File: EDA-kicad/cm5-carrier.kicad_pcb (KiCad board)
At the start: 6 copper layers, 82 x 155 mm, 122 parts, among them J1 USBC-4-0-CX90MW9-24P1, J2 SIM-G85D1160022HHR, J3 FINGER, J4 SJ2-35894B-SMT-TR, SW1 EG25-switch-CSS-1210MC, SW2 MIC-switch-CSS-1210MC, SW3 CAM-switch-CSS-1210MC, SW4 PROG, SW5 VOL-, SW6 VOL+, SW7 POW, U10 Flash-LED-Lumiled, U2 EG25GGC-128-SGNS, U3 CODEC-TLV320AIC3204IRHBR, U4 BQ25792RQMR, U5 TPS650250RHBR, U6 BAT-CONNECTOR-FLTS22WR00, U7 22V-boost-AP3032KTR-G1, U8 MP3429GL-Z, U9 FPC15pin-1mm-pitch-F52Q-1A7H1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

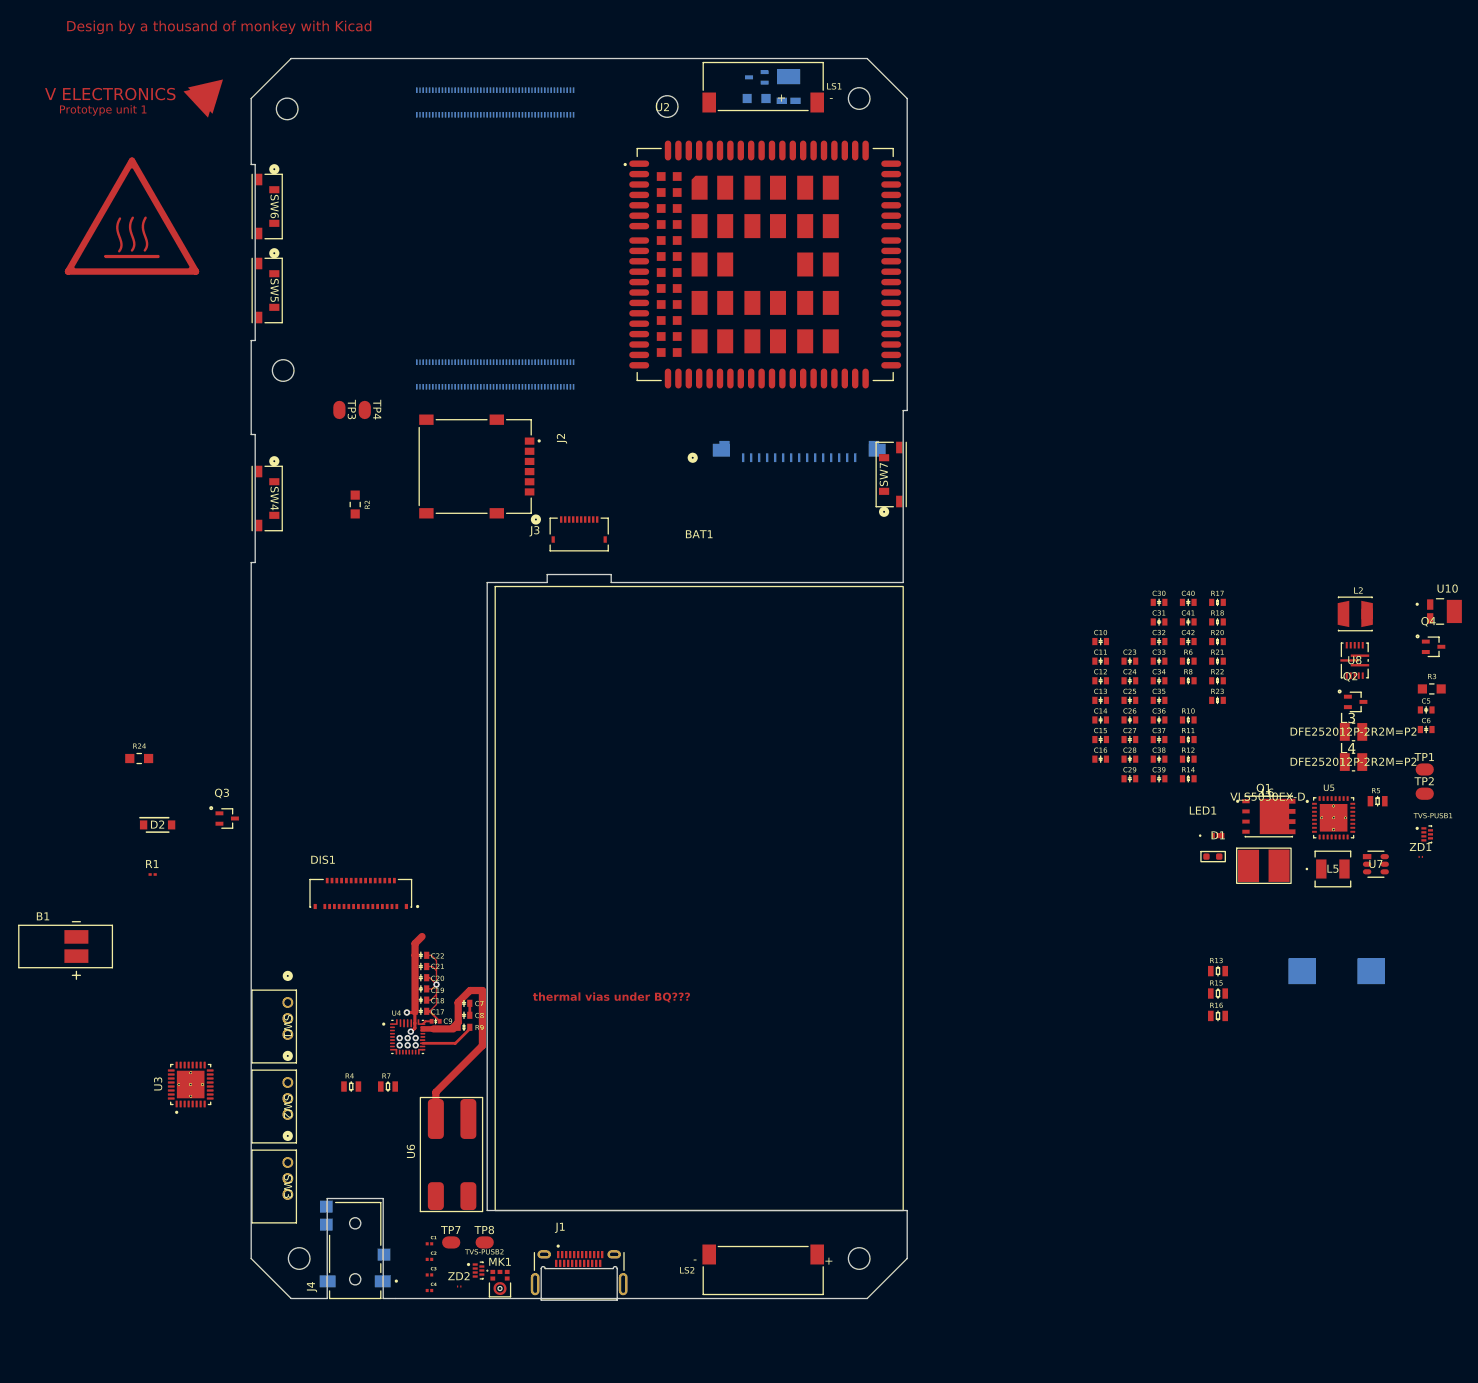
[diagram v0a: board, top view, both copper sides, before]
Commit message: charger 50% routed
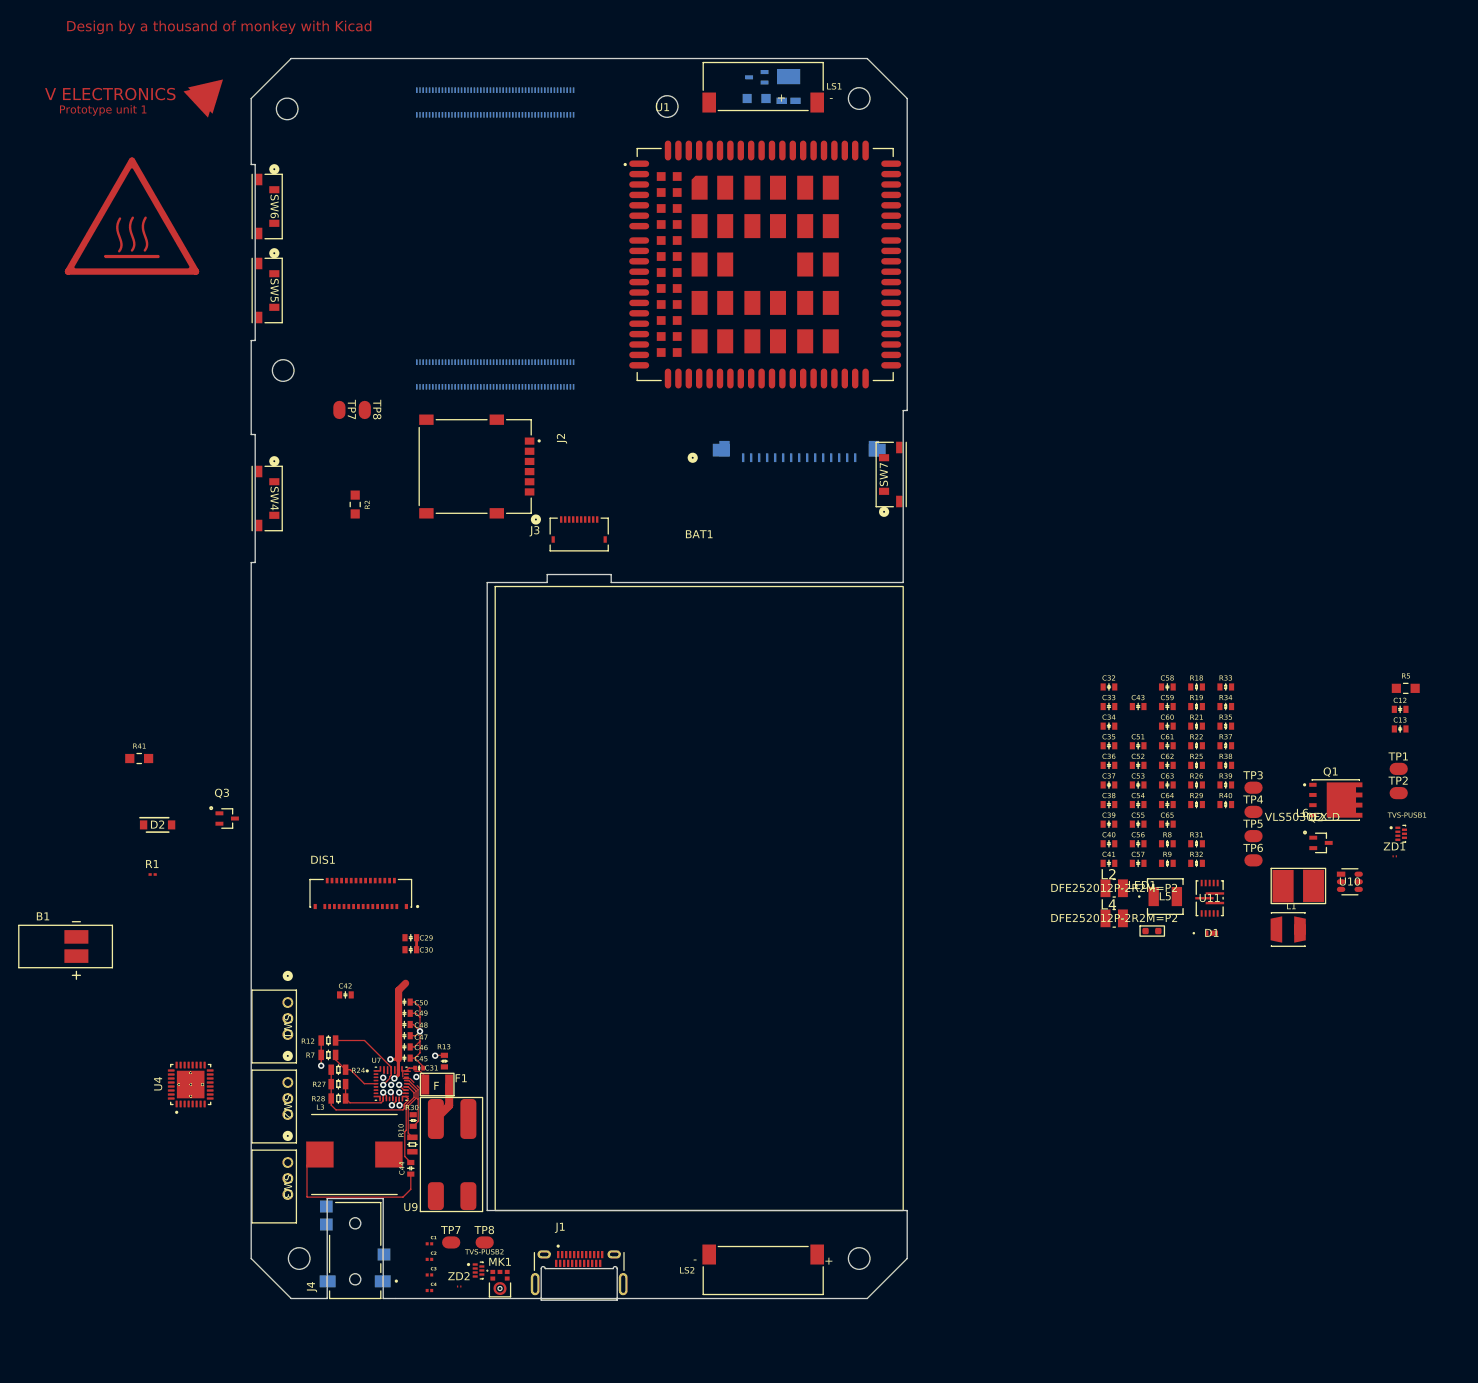
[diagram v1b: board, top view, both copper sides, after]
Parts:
- removed C10: 4.7μF, SPIRIT-footprints:0603-capacitor
- removed C11: 0.1μF, SPIRIT-footprints:0603-capacitor
- removed C14, C24, C25, C26, C27, C28: 10μF, SPIRIT-footprints:0603-capacitor
- removed C15, C16: 47nF, SPIRIT-footprints:0603-capacitor
- removed C23: 1μF, SPIRIT-footprints:0603-capacitor
- removed the C29 at (163.8, 121.0)
- removed the C30 at (167.5, 99.0)
- removed the C31 at (167.5, 101.4)
- removed C5: 200-pf-CC0603KRX7R7BB104, SPIRIT-footprints:0603-capacitor
- removed C6: 01-uf-CC0603KRX7R7BB104, SPIRIT-footprints:0603-capacitor
- removed the Q4 at (201.8, 104.5)
- removed R11: 1M, SPIRIT-footprints:0603-resistor
- removed the R12 at (171.1, 118.6)
- removed the R13 at (174.8, 145.1)
- removed R14: 10k, SPIRIT-footprints:0603-resistor
- removed R15: 10k, SPIRIT-footprints:0805-resistor
- removed R16: 30k, SPIRIT-footprints:0805-resistor
- removed R17: 680, SPIRIT-footprints:0603-resistor
- removed R20: 5, SPIRIT-footprints:0603-resistor
- removed R23: 6.8k, SPIRIT-footprints:0603-resistor
- removed R3: 100K-0805-resistor-ERA6AEB104V, SPIRIT-footprints:100K-0805-resistor-RES_ERA6AEB104V
- removed R6: 820k, SPIRIT-footprints:0603-resistor
- removed U5: TPS650250RHBR, SPIRIT-footprints:TPS650250-IC_ADS125H01IRHBT
- removed the U7 at (194.6, 131.7)
- removed U8: MP3429GL-Z, SPIRIT-footprints:QFN-3x4_MP3429_MNP
- added C43: 22uF, SPIRIT-footprints:0603-capacitor, F.Cu at (164.9, 112.0)
- added C44: 47nF, SPIRIT-footprints:0603-capacitor, F.Cu at (74.0, 169.7)
- added C51: 22uF, SPIRIT-footprints:0603-capacitor, F.Cu at (164.9, 116.9)
- added C52: 4.7uF, SPIRIT-footprints:0603-capacitor, F.Cu at (164.9, 119.4)
- added C53: 1uF, SPIRIT-footprints:0603-capacitor, F.Cu at (164.9, 121.8)
- added C54: 1uF, SPIRIT-footprints:0603-capacitor, F.Cu at (164.9, 124.3)
- added C55: 0.1uF, SPIRIT-footprints:0603-capacitor, F.Cu at (164.9, 126.7)
- added C56: 22uF, SPIRIT-footprints:0603-capacitor, F.Cu at (164.9, 129.2)
- added C57: 22uF, SPIRIT-footprints:0603-capacitor, F.Cu at (164.9, 131.6)
- added C58: 22uF, SPIRIT-footprints:0603-capacitor, F.Cu at (168.5, 109.6)
- added C59: 0.1uF, SPIRIT-footprints:0603-capacitor, F.Cu at (168.5, 112.0)
- added C60: 22uF, SPIRIT-footprints:0603-capacitor, F.Cu at (168.5, 114.5)
- added C61: 22uF, SPIRIT-footprints:0603-capacitor, F.Cu at (168.5, 116.9)
- added C62: 22uF, SPIRIT-footprints:0603-capacitor, F.Cu at (168.5, 119.4)
- added C63: 6.8nF, SPIRIT-footprints:0603-capacitor, F.Cu at (168.5, 121.8)
- added C64: 4.7uF, SPIRIT-footprints:0603-capacitor, F.Cu at (168.5, 124.3)
- added C65: 22uF, SPIRIT-footprints:0603-capacitor, F.Cu at (168.5, 126.7)
- added F1: 9A 6V, SPIRIT-footprints:PTC RESET FUSE 9.0A 6V 1210 1210L900SLPR, F.Cu at (77.2, 161.1)
- added R19: 680kΩ 1%, SPIRIT-footprints:0603-resistor, F.Cu at (172.2, 112.0)
- added R24: 5.23kΩ, SPIRIT-footprints:0805-resistor, F.Cu at (64.9, 157.4)
- added R25: 10kΩ, SPIRIT-footprints:0603-resistor, F.Cu at (172.2, 119.4)
- added R26: 470kΩ 1%, SPIRIT-footprints:0603-resistor, F.Cu at (172.2, 121.8)
- added R27: 10kΩ, SPIRIT-footprints:0805-resistor, F.Cu at (64.9, 159.2)
- added R28: 30kΩ, SPIRIT-footprints:0805-resistor, F.Cu at (64.9, 161.0)
- added R29: 680Ω, SPIRIT-footprints:0603-resistor, F.Cu at (172.2, 124.3)
- added R30: 10kΩ, SPIRIT-footprints:0603-resistor, F.Cu at (74.2, 163.8)
- added R31: 100kΩ, SPIRIT-footprints:0603-resistor, F.Cu at (172.2, 129.2)
- added R32: 100kΩ, SPIRIT-footprints:0603-resistor, F.Cu at (172.2, 131.6)
- added R33: 100kΩ, SPIRIT-footprints:0603-resistor, F.Cu at (175.8, 109.6)
- added R34: 820kΩ, SPIRIT-footprints:0603-resistor, F.Cu at (175.8, 112.0)
- added R35: 182KΩ, SPIRIT-footprints:0603-resistor, F.Cu at (175.8, 114.5)
- added R37: 5Ω, SPIRIT-footprints:0603-resistor, F.Cu at (175.8, 116.9)
- added R38: 750kΩ, SPIRIT-footprints:0603-resistor, F.Cu at (175.8, 119.4)
- added R39: 200kΩ, SPIRIT-footprints:0603-resistor, F.Cu at (175.8, 121.8)
- added R40: 6.8kΩ, SPIRIT-footprints:0603-resistor, F.Cu at (175.8, 124.3)
- added R9: 10k, SPIRIT-footprints:0603-resistor, F.Cu at (168.5, 131.6)
- added TP3: test-pad-1, SPIRIT-footprints:test-pad-1, F.Cu at (179.3, 121.1)
- added TP4: test-pad-1, SPIRIT-footprints:test-pad-1, F.Cu at (179.3, 124.2)
- added TP5: test-pad-1, SPIRIT-footprints:test-pad-1, F.Cu at (179.3, 127.2)
- added TP6: test-pad-1, SPIRIT-footprints:test-pad-1, F.Cu at (179.3, 130.2)
- added U11: MP3429GL-Z, SPIRIT-footprints:QFN-3x4_MP3429_MNP, F.Cu at (173.8, 136.0)
- C12: value 10μF -> 200pF
- C13: value 10μF -> 0.1uF
- C29: renamed from C7; value 10μF -> 10uF
- C30: renamed from C8; value 10μF -> 10uF
- C32: value 0.1μF -> 1uF
- C33, C34, C35, C39: value 22μF -> 10uF
- C36: value 0.1μF -> 22uF
- C37: value 22μF -> 4.7uF
- C38: value 22μF -> 0.1uF
- C40: value 6.8nF -> 10uF
- C41: value 4.7μF -> 10uF
- C42: value 22μF -> 47nF
- C45: renamed from C17; value 0.1μF -> 0.1uF
- C46: renamed from C18; value 10μF -> 10uF
- C47: renamed from C19; value 10μF -> 10uF
- C48: renamed from C20; value 10μF -> 10uF
- C49: renamed from C21; value 10μF -> 10uF
- C50: renamed from C22; value 10μF -> 10uF
- L1: value 2.2uH -> 3.3uH; footprint SPIRIT-footprints:2-2uh-inductorIND_ETQP4M2R2KVC -> SPIRIT-footprints:3-3uH-MURATA_LQH44PN3R3MPRL; moved to F.Cu
- L2: value 3.3uH -> 2.2uH; footprint SPIRIT-footprints:3-3uH-MURATA_LQH44PN3R3MPRL -> SPIRIT-footprints:2-2uH-inductor-INDC2520X120N
- L3: footprint SPIRIT-footprints:2-2uH-inductor-INDC2520X120N -> SPIRIT-footprints:2-2uh-inductorIND_ETQP4M2R2KVC
- R10: value 182K -> 4.7KΩ; footprint SPIRIT-footprints:0603-resistor -> SPIRIT-footprints:0805-resistor
- R12: renamed from R7; value 100k -> 100kΩ
- R13: renamed from R9; value 100 -> 100Ω
- R18: value 10k -> 100kΩ
- R2: value 270K-05W-0805-RES_ERJP06J102V -> 270KΩ 0.5W
- R21: value 750k -> 470kΩ 1%
- R22: value 200k -> 1MΩ 1%
- R41: renamed from R24; value 1K-05W-0805-RES_ERJP06J102V -> 1KΩ 0.5W
- R42: renamed from R25; value 1K -> 1KΩ 0.5W
- R5: value 4.7K -> 100KΩ; footprint SPIRIT-footprints:0805-resistor -> SPIRIT-footprints:100K-0805-resistor-RES_ERA6AEB104V
- R7: renamed from R4; value 127k -> 127kΩ
- R8: value 47k -> 10k
- U10: value Flash-LED-Lumiled -> 22V-boost-AP3032KTR-G1; footprint SPIRIT-footprints:LUMILED-DIODFN449X305X210-3N -> SPIRIT-footprints:SOT23-6_DIO
- moved L3 135.6 mm to (66.9, 168.0)
- moved C42 114.2 mm to (65.8, 148.1)
- moved R10 110.6 mm to (74.2, 166.8), turned to 90 degrees
- moved L2 45.6 mm to (161.9, 134.7)
- moved C12 37.6 mm to (197.6, 112.4)
- moved C13 37.6 mm to (197.6, 114.8)
- moved U10 35.8 mm to (191.3, 133.9)
- moved L4 35.7 mm to (161.9, 138.5)
- moved C40 31.8 mm to (161.2, 129.2)
- moved C41 31.8 mm to (161.2, 131.6)
- moved L5 21.2 mm to (168.3, 135.8)
- moved R8 20.5 mm to (168.5, 129.2)
- moved Q2 18.2 mm to (187.7, 129.1)
- moved R5 14.5 mm to (198.3, 109.7)
- moved D1 12.2 mm to (174.1, 140.3)
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- renumbered C9 to C31, TP3 to TP7, TP4 to TP8, U2 to U1, U9 to U12, U10 to U13, U3 to U4, U4 to U7, U6 to U9
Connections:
- net SCL renamed SCL CH
- net SDA renamed SDA CH
- C12 pad 1: Net-(U4-PMID) -> GND
- C12 pad 2: BACKLIGHT- -> MIC-SWITCH
- C13 pad 1: Net-(U4-PMID) -> MIC-SWITCH
- C13 pad 2: BACKLIGHT- -> GND
- C29 pad 2: BACKLIGHT- -> GND
- C30 pad 2: BACKLIGHT- -> GND
- C31 pad 2: BACKLIGHT- -> GND
- C32 pad 1: Net-(U8-BST) -> Net-(U8-VCC)
- C32 pad 2: Net-(U8-SW) -> GND
- C33 pad 1: SYS -> Net-(U8-VINDCDC1)
- C33 pad 2: BACKLIGHT- -> GND
- C34 pad 1: SYS -> Net-(U8-VINDCDC2)
- C34 pad 2: BACKLIGHT- -> GND
- C35 pad 1: SYS -> Net-(U8-VINDCDC3)
- C35 pad 2: BACKLIGHT- -> GND
- C36 pad 1: 5V -> DEFDCDC1 DIVIDER
- C36 pad 2: BACKLIGHT- -> GND
- C37 pad 1: 5V -> REGN
- C37 pad 2: BACKLIGHT- -> GND
- C38 pad 1: 5V -> Net-(U7-PMID)
- C38 pad 2: BACKLIGHT- -> GND
- C39 pad 1: 5V -> Net-(U7-PMID)
- C39 pad 2: BACKLIGHT- -> GND
- C40 pad 1: Net-(U8-COMP) -> Net-(U7-PMID)
- C40 pad 2: Net-(C40-Pad2) -> GND
- C41 pad 1: BACKLIGHT- -> Net-(U7-PMID)
- C41 pad 2: Net-(U8-VDD) -> GND
- C42 pad 1: Net-(U8-SS) -> Net-(U7-SW1)
- C42 pad 2: AGND -> Net-(U7-BTST1)
- C45 pad 2: BACKLIGHT- -> GND
- C46 pad 2: BACKLIGHT- -> GND
- C47 pad 2: BACKLIGHT- -> GND
- C48 pad 2: BACKLIGHT- -> GND
- C49 pad 2: BACKLIGHT- -> GND
- C50 pad 2: BACKLIGHT- -> GND
- DIS1 pad 1: BACKLIGHT- -> GND
- DIS1 pad 10: BACKLIGHT- -> GND
- DIS1 pad 13: BACKLIGHT- -> GND
- DIS1 pad 16: BACKLIGHT- -> GND
- DIS1 pad 19: BACKLIGHT- -> GND
- DIS1 pad 20: BACKLIGHT- -> GND
- DIS1 pad 4: BACKLIGHT- -> GND
- DIS1 pad 7: BACKLIGHT- -> GND
- J1 pad A1: BACKLIGHT- -> GND
- J1 pad A12: BACKLIGHT- -> GND
- J1 pad B1: BACKLIGHT- -> GND
- J1 pad B12: BACKLIGHT- -> GND
- J1 pad SH1: BACKLIGHT- -> GND
- J1 pad SH2: BACKLIGHT- -> GND
- J1 pad SH3: BACKLIGHT- -> GND
- J1 pad SH4: BACKLIGHT- -> GND
- J2 pad C5: BACKLIGHT- -> GND
- J2 pad S1: BACKLIGHT- -> GND
- J2 pad S2: BACKLIGHT- -> GND
- J2 pad S3: BACKLIGHT- -> GND
- J3 pad 1: BACKLIGHT- -> GND
- J4 pad 1: unconnected-(J4-Pad1) -> GND
- J4 pad 2: unconnected-(J4-Pad2) -> JACK_AUDIO_RIGHT
- J4 pad 3: unconnected-(J4-Pad3) -> JACK_AUDIO_LEFT
- J4 pad 4: unconnected-(J4-Pad4) -> JACK_MIC
- L1 pad 1: Net-(U4-SW2) -> DEFDCDC1 DIVIDER
- L1 pad 2: Net-(U4-SW1) -> Net-(U8-L1)
- L2 pad 1: 3V3A -> Net-(U8-VDCDC2)
- L3 pad 1: 1V8 -> Net-(U7-SW2)
- L3 pad 2: Net-(U5-L2) -> Net-(U7-SW1)
- L4 pad 1: 3V3B -> Net-(U8-VDCDC3)
- L6 pad 2: Net-(U8-SW) -> Net-(U11-SW)
- MK1 pad 2: BACKLIGHT- -> GND
- MK1 pad 3: BACKLIGHT- -> GND
- MK1 pad 6: AUDIO_MIC_DATA -> Net-(MK1-DATA_OUT)
- Module1 pad 1: BACKLIGHT- -> GND
- Module1 pad 107: BACKLIGHT- -> GND
- Module1 pad 108: BACKLIGHT- -> GND
- Module1 pad 113: BACKLIGHT- -> GND
- Module1 pad 114: BACKLIGHT- -> GND
- Module1 pad 119: BACKLIGHT- -> GND
- Module1 pad 120: BACKLIGHT- -> GND
- Module1 pad 125: BACKLIGHT- -> GND
- Module1 pad 126: BACKLIGHT- -> GND
- Module1 pad 13: BACKLIGHT- -> GND
- Module1 pad 131: BACKLIGHT- -> GND
- Module1 pad 132: BACKLIGHT- -> GND
- Module1 pad 137: BACKLIGHT- -> GND
- Module1 pad 138: BACKLIGHT- -> GND
- Module1 pad 14: BACKLIGHT- -> GND
- Module1 pad 144: BACKLIGHT- -> GND
- Module1 pad 150: BACKLIGHT- -> GND
- Module1 pad 155: BACKLIGHT- -> GND
- Module1 pad 156: BACKLIGHT- -> GND
- Module1 pad 161: BACKLIGHT- -> GND
- Module1 pad 162: BACKLIGHT- -> GND
- Module1 pad 167: BACKLIGHT- -> GND
- Module1 pad 168: BACKLIGHT- -> GND
- Module1 pad 173: BACKLIGHT- -> GND
- Module1 pad 174: BACKLIGHT- -> GND
- Module1 pad 179: BACKLIGHT- -> GND
- Module1 pad 180: BACKLIGHT- -> GND
- Module1 pad 185: BACKLIGHT- -> GND
- Module1 pad 186: BACKLIGHT- -> GND
- Module1 pad 191: BACKLIGHT- -> GND
- Module1 pad 192: BACKLIGHT- -> GND
- Module1 pad 197: BACKLIGHT- -> GND
- Module1 pad 198: BACKLIGHT- -> GND
- Module1 pad 2: BACKLIGHT- -> GND
- Module1 pad 22: BACKLIGHT- -> GND
- Module1 pad 23: BACKLIGHT- -> GND
- Module1 pad 25: unconnected-(Module1A-GPIO21-Pad25) -> AUDIO_SOUND_DATA
- Module1 pad 28: unconnected-(Module1A-GPIO13-Pad28) -> GPIO13
- Module1 pad 32: BACKLIGHT- -> GND
- Module1 pad 33: BACKLIGHT- -> GND
- Module1 pad 41: AUDIO_MCLK -> unconnected-(Module1A-GPIO25-Pad41)
- Module1 pad 42: BACKLIGHT- -> GND
- Module1 pad 43: BACKLIGHT- -> GND
- Module1 pad 45: unconnected-(Module1A-GPIO24-Pad45) -> AUDIO_RESET
- Module1 pad 52: BACKLIGHT- -> GND
- Module1 pad 53: BACKLIGHT- -> GND
- Module1 pad 54: GPIO4 -> AUDIO_MCLK
- Module1 pad 60: BACKLIGHT- -> GND
- Module1 pad 66: BACKLIGHT- -> GND
- Module1 pad 71: BACKLIGHT- -> GND
- Module1 pad 74: BACKLIGHT- -> GND
- Module1 pad 77: unconnected-(Module1A-+5v_(Input)-Pad77) -> 5V
- Module1 pad 79: unconnected-(Module1A-+5v_(Input)-Pad79) -> 5V
- Module1 pad 8: BACKLIGHT- -> GND
- Module1 pad 80: unconnected-(Module1A-SCL0-Pad80) -> SCL PMIC
- Module1 pad 81: unconnected-(Module1A-+5v_(Input)-Pad81) -> 5V
- Module1 pad 82: unconnected-(Module1A-SDA0-Pad82) -> SDA PMIC
- Module1 pad 83: unconnected-(Module1A-+5v_(Input)-Pad83) -> 5V
- Module1 pad 85: unconnected-(Module1A-+5v_(Input)-Pad85) -> 5V
- Module1 pad 87: unconnected-(Module1A-+5v_(Input)-Pad87) -> 5V
- Module1 pad 98: BACKLIGHT- -> GND
- Q3 pad 3: BACKLIGHT- -> GND
- Q4 pad 3: BACKLIGHT- -> GND
- R10 pad 1: BACKLIGHT- -> GND
- R10 pad 2: Net-(U5-DEFDCDC3) -> Net-(U7-PROG)
- R12 pad 2: BACKLIGHT- -> GND
- R18 pad 1: VCC -> Net-(U8-VCC)
- R18 pad 2: ~{INT} -> ~{LOW_BAT}
- R21 pad 1: 5V -> GND
- R21 pad 2: Net-(U8-FB) -> Net-(U8-PWRFAIL_SNS)
- R22 pad 1: Net-(U8-FB) -> Net-(U8-LOWBAT_SNS)
- R22 pad 2: AGND -> SYS
- R5 pad 1: BACKLIGHT- -> GND
- R5 pad 2: Net-(U4-PROG) -> Net-(MK1-DATA_OUT)
- R8 pad 1: 3V3 -> SCL PMIC
- R8 pad 2: ~{PWRFAIL} -> 3V3B
- SW2 pad 1: 3V3B -> 1V8
- TVS-PUSB1 pad 2: BACKLIGHT- -> GND
- U10 pad 1: Net-(Q4-D) -> Net-(D1-A)
- U10 pad 2: VCC -> GND
- U10 pad 3: (no net) -> BACKLIGHT-
- U12 pad 1: BACKLIGHT- -> GND
- U12 pad 10: BACKLIGHT- -> GND
- U12 pad 4: BACKLIGHT- -> GND
- U4 pad 12: unconnected-(U3-SPI_SELECT-Pad12) -> GND
- U4 pad 13: unconnected-(U3-IN1_L-Pad13) -> Net-(U4-IN1_L)
- U4 pad 14: unconnected-(U3-IN1_R-Pad14) -> Net-(U4-IN1_R)
- U4 pad 17: BACKLIGHT- -> GND
- U4 pad 18: unconnected-(U3-REF-Pad18) -> Net-(U4-REF)
- U4 pad 19: unconnected-(U3-MICBIAS-Pad19) -> Net-(U4-MICBIAS)
- U4 pad 21: unconnected-(U3-IN3_R-Pad21) -> Net-(U4-IN3_R)
- U4 pad 22: unconnected-(U3-LOL-Pad22) -> AMP_AUDIO_LEFT
- U4 pad 23: unconnected-(U3-LOR-Pad23) -> AMP_AUDIO_RIGHT
- U4 pad 24: VCC -> 1V8
- U4 pad 25: unconnected-(U3-HPL-Pad25) -> Net-(U4-HPL)
- U4 pad 26: unconnected-(U3-LDOIN/HPVDD-Pad26) -> 3V3B
- U4 pad 27: unconnected-(U3-HPR-Pad27) -> Net-(U4-HPR)
- U4 pad 28: BACKLIGHT- -> GND
- U4 pad 29: unconnected-(U3-DVDD-Pad29) -> 1V8
- U4 pad 30: unconnected-(U3-LDO_SELECT-Pad30) -> 3V3B
- U4 pad 31: unconnected-(U3-~{RESET}-Pad31) -> AUDIO_RESET
- U4 pad 33: unconnected-(U3-EP-Pad33) -> GND
- U4 pad 4: unconnected-(U3-DIN/MFP1-Pad4) -> AUDIO_SOUND_DATA
- U4 pad 5: unconnected-(U3-DOUT/MFP2-Pad5) -> AUDIO_MIC_DATA
- U4 pad 6: unconnected-(U3-IOVDD-Pad6) -> 3V3B
- U4 pad 7: BACKLIGHT- -> GND
- U4 pad 8: unconnected-(U3-SCLK/MFP3-Pad8) -> JACK_MIC
- U7 pad 10: BACKLIGHT- -> GND
- U7 pad 11: BACKLIGHT- -> GND
- U7 pad 20: Net-(U4-PROG) -> Net-(U7-PROG)
- U7 pad 21: ~{INT} -> ~{BQ INT}
- U7 pad 26: Net-(U4-SW2) -> Net-(U7-SW2)
- U7 pad 27: BACKLIGHT- -> GND
- U7 pad 28: Net-(U4-SW1) -> Net-(U7-SW1)
- U7 pad 29: Net-(U4-PMID) -> Net-(U7-PMID)
- U7 pad 4: Net-(U4-BTST1) -> Net-(U7-BTST1)
- U9 pad 3: BAT+ -> Net-(U9-OUT+)
- U9 pad 4: BACKLIGHT- -> GND
- ZD1 pad 2: BACKLIGHT- -> GND
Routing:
- net GND: track 0.00 -> 37.8 mm, vias 0 -> 3
- net BAT+: track 28.0 -> 0.00 mm, vias 0 -> 1
- net Net-(U7-SW2): track 0.00 -> 21.5 mm
- net BACKLIGHT-: track 17.9 -> 0.00 mm, vias 1 -> 0
- net Net-(U7-TS): track 0.00 -> 15.7 mm
- net Net-(U7-ILIM_HIZ): track 0.00 -> 15.7 mm, vias 0 -> 2
- net Net-(U7-BTST2): track 0.00 -> 10.8 mm
- net Net-(U7-PROG): track 0.00 -> 7.99 mm, vias 0 -> 1
- net REGN: track 0.00 -> 6.89 mm
- net ~{BQ INT}: track 0.00 -> 6.77 mm
- net Net-(U9-OUT+): track 0.00 -> 5.00 mm
- net Net-(U7-BATP): track 6.64 -> 8.40 mm, vias 0 -> 2
- net SDA CH: track 0.00 -> 1.13 mm, vias 0 -> 1
- net SCL CH: track 0.00 -> 1.01 mm, vias 0 -> 1
- net ~{CE}: track 0.00 -> 0.95 mm, vias 0 -> 1
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- added copper zone on In2.Cu, net AGND
- added copper zone on In4.Cu, net AGND
- added copper zone on F.Cu, net BAT+
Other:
- board text removed: "thermal vias under BQ???"

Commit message: routed charger
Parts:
- moved R25 109.5 mm to (67.2, 150.5)
- moved R29 107.8 mm to (67.2, 149.0), turned to 180 degrees
- moved LED1 99.2 mm to (66.8, 152.6)
- moved C37 97.5 mm to (67.2, 147.6)
- moved C38 94.5 mm to (70.5, 150.7), turned to 180 degrees
- moved C39 93.5 mm to (70.5, 149.2), turned to 180 degrees
- moved C40 92.6 mm to (70.5, 147.8), turned to 180 degrees
- moved C41 91.9 mm to (70.5, 146.3), turned to 180 degrees
- moved L5 20.3 mm to (182.8, 149.9)
- moved L4 18.5 mm to (171.4, 154.3)
- moved L2 16.3 mm to (167.9, 149.8)
- moved TP8 10.7 mm to (83.0, 188.7)
- moved TP7 10.5 mm to (78.0, 188.4)
- moved C42 7.16 mm to (68.5, 154.7), turned to 180 degrees
- moved J1 0.20 mm to (95.0, 184.0)
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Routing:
- net D+: track 0.00 -> 43.9 mm, vias 0 -> 2
- net D-: track 0.00 -> 42.7 mm, vias 0 -> 2
- net Net-(U7-SW1): track 0.00 -> 21.9 mm, vias 0 -> 2
- net Net-(U7-PMID): track 0.00 -> 12.7 mm, vias 0 -> 2
- net REGN: track 6.89 -> 16.4 mm
- net Net-(LED1-K): track 0.00 -> 8.36 mm
- net Net-(U7-BTST1): track 0.00 -> 6.57 mm
- net SYS: track 16.5 -> 10.8 mm, vias 2 -> 3
- net GND: track 37.8 -> 42.9 mm, vias 3 -> 4
- net Net-(LED1-A): track 0.00 -> 5.01 mm
- net USBC POW: track 0.00 -> 2.09 mm, vias 0 -> 3
- net Net-(U7-SW2): track 21.5 -> 22.6 mm, vias 0 -> 2
- net Net-(U7-PROG): vias 1 -> 0
- net (no net): vias 1 -> 0
- added copper zone on F.Cu, net SYS
- added copper zone on In1.Cu, net SYS
- added copper zone on F.Cu, net USBC POW
- added copper zone on In1.Cu, net USBC POW
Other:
- board text added: "calculate d+ d-"
